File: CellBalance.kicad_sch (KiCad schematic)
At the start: 8 parts, among them Q1 GSF3400

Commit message: mostly done afe ic
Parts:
- removed C1: 10nF, symbol Device:C_Small
- removed D1: BZT52B3V9-AQ, footprints:P35_SOD-123F, symbol symbols:Diode
- removed Q1: GSF3400, Package_TO_SOT_SMD:SOT-23-3, symbol symbols:GSF3400
- removed R1, R2: 52.3, symbol Device:R_Small_US
- removed R3, R4: 1k, symbol Device:R_Small_US
- removed R5: 2k, symbol Device:R_Small_US
- added C4: 1nF, symbol Device:C_Small
- added C5: 330nF, symbol Device:C_Small
- added D3: BZT52B3V9-AQ, footprints:P35_SOD-123F, symbol symbols:Diode
- added GSF2: MOSFET, P-CH, SINGLE, -4.1A, -30, Package_TO_SOT_SMD:SOT-23-3, symbol symbols:GSF0304
- added R11, R12: 52.3k, symbol Device:R_Small_US
- added R13: 10, symbol Device:R_Small_US
- added R14: 8.3, symbol Device:R_Small_US
- added R15: 2k, symbol Device:R_Small_US
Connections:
- net Battery_Bottom: now also C4.1, R11.2, R12.2, R13.1
- net Battery_Top: now also GSF2.2 (S), R14.2
- net Monitor_Bottom: now also C5.2, R13.2, R15.1
- net Monitor_Top: now also C5.1, D3.2 (C), GSF2.1 (G), R14.1, R15.2
- new net: D3.1 (A), GSF2.3 (D), R11.1, R12.1
- new net GNDREF: C4.2
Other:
- note added: "C2 is C_F, 330nF taken from typical application"
- note added: "C3 = C_EMC (i used typical application)"
- note added: "R6/R7 is R_balance"
- note added: "the typical application didn't include the zener or the current limiting resistor i just included it to clamp vgs"

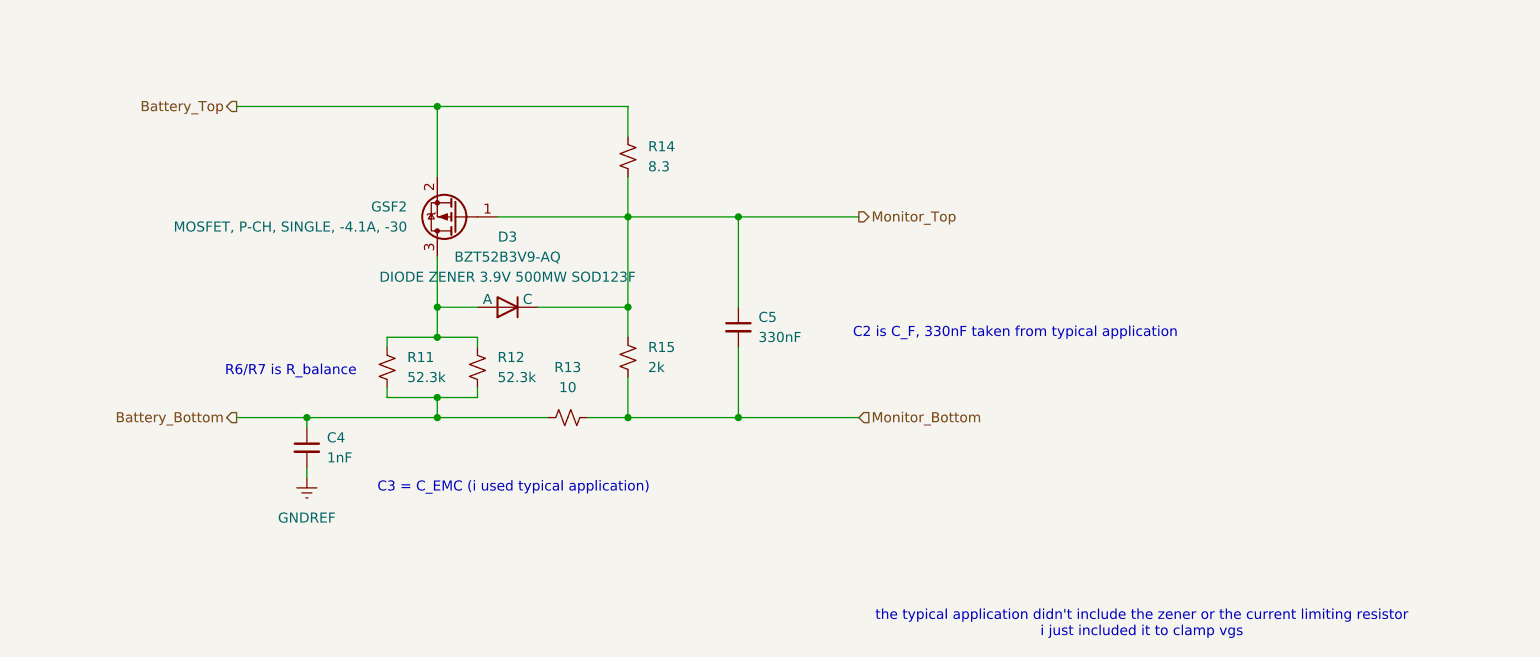
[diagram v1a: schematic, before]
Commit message: fixed balancing module and added pulse transformer
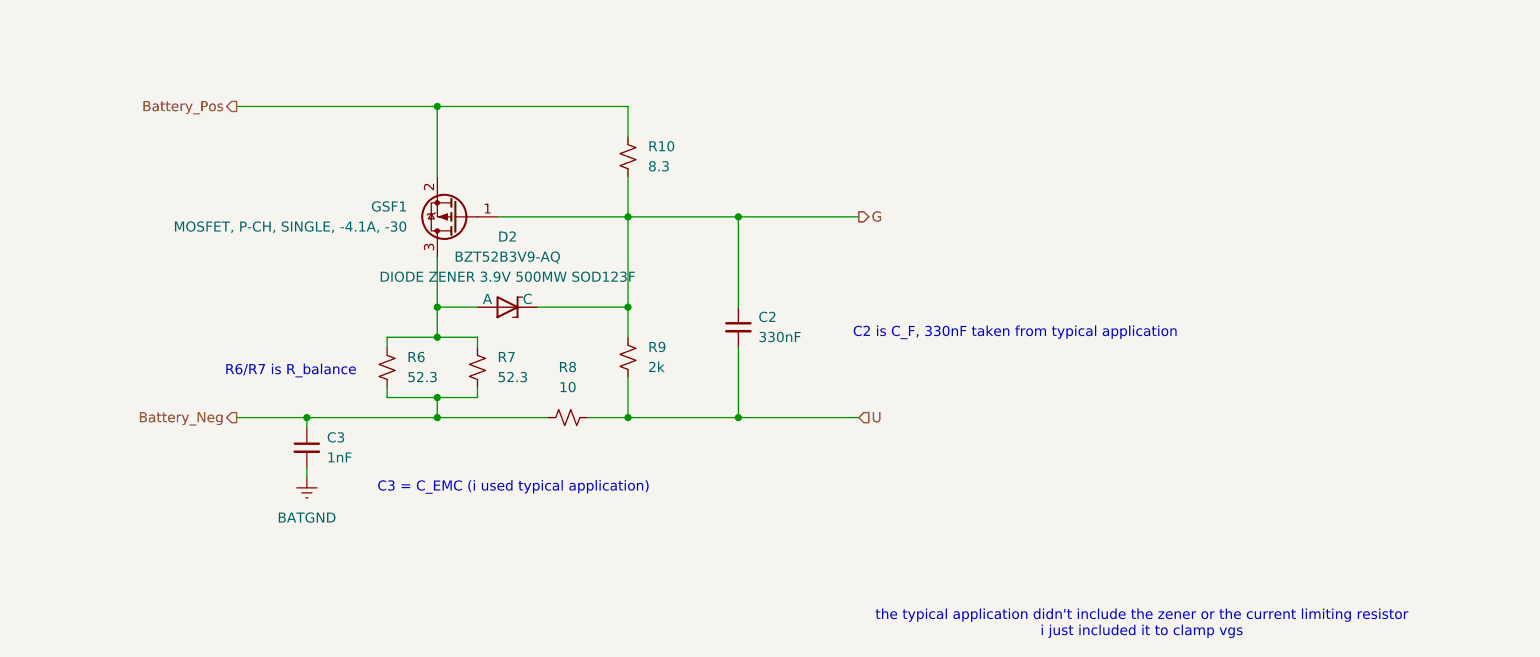
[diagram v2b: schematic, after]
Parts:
- R6: renamed from R11; value 52.3k -> 52.3
- R7: renamed from R12; value 52.3k -> 52.3
- renumbered C5 to C2, C4 to C3, D3 to D2, GSF2 to GSF1, R14 to R10, R13 to R8, R15 to R9
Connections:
- net Battery_Bottom renamed Battery_Neg
- net Battery_Top renamed Battery_Pos
- net GNDREF renamed BATGND
- net Monitor_Bottom renamed U
- net Monitor_Top renamed G

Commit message: finished schematic
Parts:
- removed D2: BZT52B3V9-AQ, footprints:P35_SOD-123F, symbol symbols:Diode
- removed R10: 8.3, symbol Device:R_Small_US
- removed R9: 2k, symbol Device:R_Small_US
- added R8: 8.3, symbol Device:R_Small_US
- C11: renamed from C2; value 330nF -> 100nF
- renumbered C3 to C10, R8 to R9
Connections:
- net Battery_Pos: now also R8.2
- net G: now also R8.1
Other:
- note added: "C2 is C_F, 100nF taken from typical application"
- note removed: "C2 is C_F, 330nF taken from typical application"
- moved on the sheet: C11, GSF1

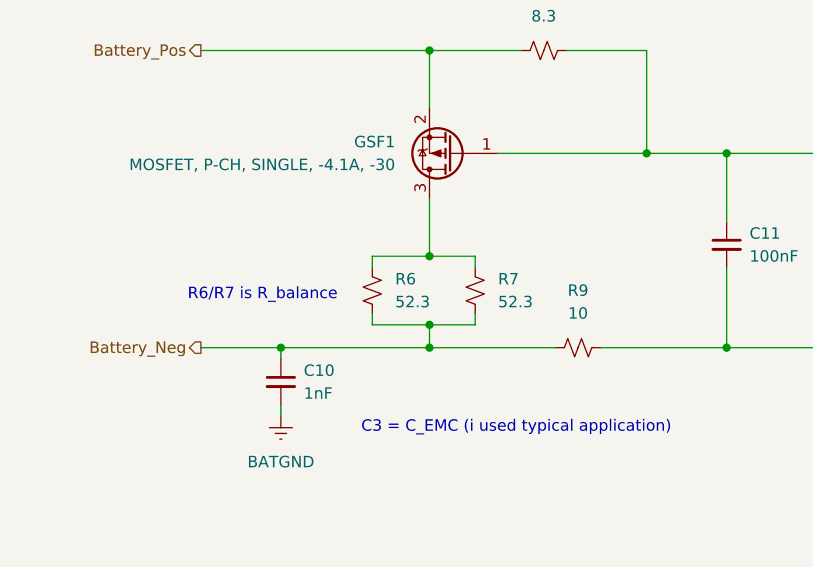
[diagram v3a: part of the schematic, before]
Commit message: added leds and updated library
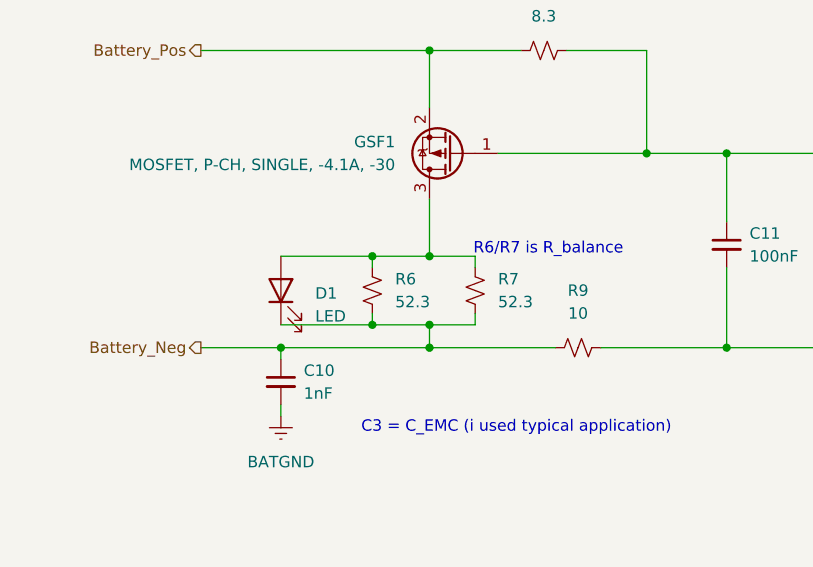
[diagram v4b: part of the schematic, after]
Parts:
- added D1: LED, symbol Device:LED
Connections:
- net Battery_Neg: now also D1.1 (K)
- net at GSF1.3 (D), R6.1, R7.1: now also D1.2 (A)
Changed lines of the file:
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@@
 	(text "R6/R7 is R_balance"
 		(exclude_from_sim no)
-		(at 117.348 99.568 0)
+		(at 149.098 94.488 0)
 		(effects
 			(font
@@
 	)
 	(junction
+		(at 129.54 95.25)
+		(diameter 0)
+		(color 0 0 0 0)
+	)
+	(junction
 		(at 119.38 105.41)
 		(diameter 0)
@@
 	)
 	(junction
+		(at 129.54 102.87)
+		(diameter 0)
+		(color 0 0 0 0)
+	)
+	(junction
 		(at 160.02 83.82)
 		(diameter 0)
@@
 	(wire
 		(pts
+			(xy 119.38 102.87) (xy 129.54 102.87)
+		)
+		(stroke
+			(width 0)
+			(type default)
+		)
+	)
+	(wire
+		(pts
 			(xy 110.49 72.39) (xy 135.89 72.39)
 		)
@@
 		(pts
 			(xy 154.94 105.41) (xy 168.91 105.41)
+		)
+		(stroke
+			(width 0)
+			(type default)
+		)
+	)
+	(wire
+		(pts
+			(xy 119.38 95.25) (xy 129.54 95.25)
 		)
 		(stroke
@@
 					(unit 1)
 				)
+			)
+		)
+	)
+	(symbol
+		(lib_id "Device:LED")
+		(at 119.38 99.06 90)
+		(unit 1)
+		(body_style 1)
+		(exclude_from_sim no)
+		(in_bom yes)
+		(on_board yes)
+		(in_pos_files yes)
+		(dnp no)
+		(fields_autoplaced yes)
+		(property "Reference" "D1"
+			(at 123.19 99.3774 90)
+			(show_name no)
+			(do_not_autoplace no)
+			(effects
+				(font
+					(size 1.27 1.27)
+				)
+				(justify right)
+			)
+		)
+		(property "Value" "LED"
+			(at 123.19 101.9174 90)
+			(show_name no)
+			(do_not_autoplace no)
+			(effects
+				(font
+					(size 1.27 1.27)
+				)
+				(justify right)
+			)
+		)
+		(property "Footprint" ""
+			(at 119.38 99.06 0)
+			(hide yes)
+			(show_name no)
+			(do_not_autoplace no)
+			(effects
+				(font
+					(size 1.27 1.27)
+				)
+			)
+		)
+		(property "Datasheet" "https://www.digikey.ca/en/products/detail/para-light/LC295JRWDT-5A-U1/26692441"
+			(at 119.38 99.06 0)
+			(hide yes)
+			(show_name no)
+			(do_not_autoplace no)
+			(effects
+				(font
+					(size 1.27 1.27)
+				)
+			)
+		)
+		(property "Description" "Light emitting diode"
+			(at 119.38 99.06 0)
+			(hide yes)
+			(show_name no)
+			(do_not_autoplace no)
+			(effects
+				(font
+					(size 1.27 1.27)
+				)
+			)
+		)
+		(property "Sim.Pins" "1=K 2=A"
+			(at 119.38 99.06 0)
+			(hide yes)
+			(show_name no)
+			(do_not_autoplace no)
+			(effects
+				(font
+					(size 1.27 1.27)
+				)
+			)
+		)
+		(pin "1"
+		)
+		(pin "2"
+		)
+		(instances
+			(project "bms-afe"
+				(path "/226a23e7-09bb-40bc-b53a-ec42a6b7cc90/199aea63-5bfb-41be-ba55-0a021bc0a074"
+					(reference "D3")
+					(unit 1)
+				)
+				(path "/226a23e7-09bb-40bc-b53a-ec42a6b7cc90/2aa084bd-01e7-47e5-8f6d-30b4f325d7f4"
+					(reference "D2")
+					(unit 1)
+				)
+				(path "/226a23e7-09bb-40bc-b53a-ec42a6b7cc90/30f9ba51-47e3-4adb-895f-80ddd8089ec1"
+					(reference "D5")
+					(unit 1)
+				)
+				(path "/226a23e7-09bb-40bc-b53a-ec42a6b7cc90/9ef805d4-1601-4480-b9fd-3e26be539576"
+					(reference "D6")
+					(unit 1)
+				)
+				(path "/226a23e7-09bb-40bc-b53a-ec42a6b7cc90/a6f93463-0553-4e94-825f-86704d73fcd7"
+					(reference "D1")
+					(unit 1)
+				)
+				(path "/226a23e7-09bb-40bc-b53a-ec42a6b7cc90/cf97efbe-7ee9-4abe-8844-0d879c082204"
+					(reference "D4")
+					(unit 1)
+				)

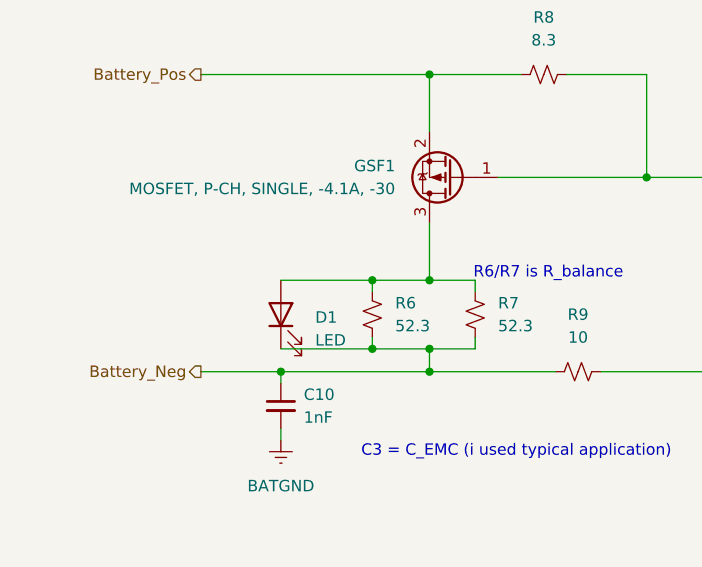
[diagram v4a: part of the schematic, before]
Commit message: added led resistor
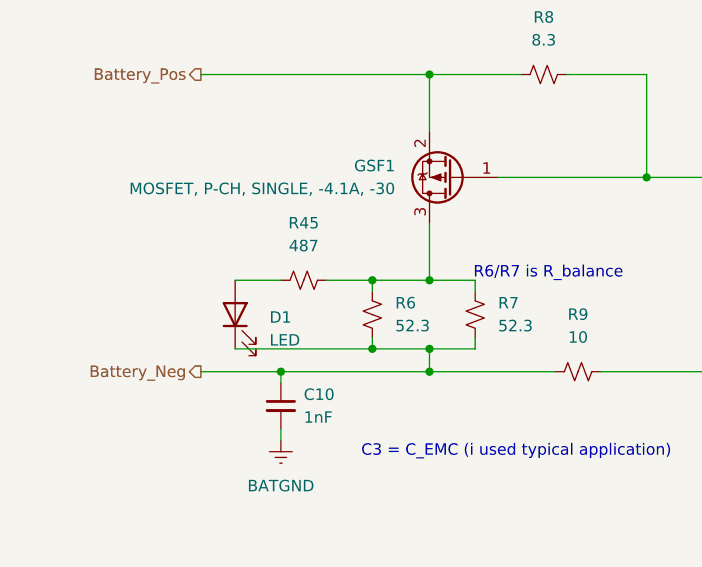
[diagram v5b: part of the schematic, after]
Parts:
- added R45: 487, symbol Device:R_Small_US
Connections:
- net at GSF1.3 (D), R6.1, R7.1: now also R45.2; no longer D1.2 (A)
- new net: D1.2 (A), R45.1
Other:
- moved on the sheet: D1
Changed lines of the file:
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@@
+	)
+	(junction
+		(at 119.38 105.41)
+		(diameter 0)
+		(color 0 0 0 0)
+	)
+	(junction
+		(at 135.89 105.41)
+		(diameter 0)
+		(color 0 0 0 0)
+	)
+	(junction
+		(at 129.54 102.87)
+		(diameter 0)
+		(color 0 0 0 0)
+	)
+	(junction
+		(at 160.02 83.82)
+		(diameter 0)
+		(color 0 0 0 0)
 	)
 	(junction
@@
 		(color 0 0 0 0)
 	)
-	(junction
-		(at 119.38 105.41)
-		(diameter 0)
-		(color 0 0 0 0)
-	)
-	(junction
-		(at 135.89 105.41)
-		(diameter 0)
-		(color 0 0 0 0)
-	)
-	(junction
-		(at 129.54 102.87)
-		(diameter 0)
-		(color 0 0 0 0)
-	)
-	(junction
-		(at 160.02 83.82)
-		(diameter 0)
-		(color 0 0 0 0)
-	)
 	(wire
 		(pts
@@
 	(wire
 		(pts
-			(xy 119.38 102.87) (xy 129.54 102.87)
+			(xy 114.3 102.87) (xy 129.54 102.87)
 		)
 		(stroke
@@
 	(wire
 		(pts
-			(xy 119.38 95.25) (xy 129.54 95.25)
+			(xy 114.3 95.25) (xy 119.38 95.25)
 		)
 		(stroke
@@
 		(pts
 			(xy 168.91 83.82) (xy 168.91 91.44)
+		)
+		(stroke
+			(width 0)
+			(type default)
+		)
+	)
+	(wire
+		(pts
+			(xy 124.46 95.25) (xy 129.54 95.25)
 		)
 		(stroke
@@
 	)
 	(symbol
+		(lib_id "Device:R_Small_US")
+		(at 121.92 95.25 90)
+		(unit 1)
+		(body_style 1)
+		(exclude_from_sim no)
+		(in_bom yes)
+		(on_board yes)
+		(in_pos_files yes)
+		(dnp no)
+		(fields_autoplaced yes)
+		(property "Reference" "R45"
+			(at 121.92 88.9 90)
+			(show_name no)
+			(do_not_autoplace no)
+			(effects
+				(font
+					(size 1.27 1.27)
+				)
+			)
+		)
+		(property "Value" "487"
+			(at 121.92 91.44 90)
+			(show_name no)
+			(do_not_autoplace no)
+			(effects
+				(font
+					(size 1.27 1.27)
+				)
+			)
+		)
+		(property "Footprint" ""
+			(at 121.92 95.25 0)
+			(hide yes)
+			(show_name no)
+			(do_not_autoplace no)
+			(effects
+				(font
+					(size 1.27 1.27)
+				)
+			)
+		)
+		(property "Datasheet" ""
+			(at 121.92 95.25 0)
+			(hide yes)
+			(show_name no)
+			(do_not_autoplace no)
+			(effects
+				(font
+					(size 1.27 1.27)
+				)
+			)
+		)
+		(property "Description" "Resistor, small US symbol"
+			(at 121.92 95.25 0)
+			(hide yes)
+			(show_name no)
+			(do_not_autoplace no)
+			(effects
+				(font
+					(size 1.27 1.27)
+				)
+			)
+		)
+		(pin "2"
+		)
+		(pin "1"
+		)
+		(instances
+			(project "bms-afe"
+				(path "/226a23e7-09bb-40bc-b53a-ec42a6b7cc90/199aea63-5bfb-41be-ba55-0a021bc0a074"
+					(reference "R47")
+					(unit 1)
+				)
+				(path "/226a23e7-09bb-40bc-b53a-ec42a6b7cc90/2aa084bd-01e7-47e5-8f6d-30b4f325d7f4"
+					(reference "R46")
+					(unit 1)
+				)
+				(path "/226a23e7-09bb-40bc-b53a-ec42a6b7cc90/30f9ba51-47e3-4adb-895f-80ddd8089ec1"
+					(reference "R49")
+					(unit 1)
+				)
+				(path "/226a23e7-09bb-40bc-b53a-ec42a6b7cc90/9ef805d4-1601-4480-b9fd-3e26be539576"
+					(reference "R50")
+					(unit 1)
+				)
+				(path "/226a23e7-09bb-40bc-b53a-ec42a6b7cc90/a6f93463-0553-4e94-825f-86704d73fcd7"
+					(reference "R45")
+					(unit 1)
+				)
+				(path "/226a23e7-09bb-40bc-b53a-ec42a6b7cc90/cf97efbe-7ee9-4abe-8844-0d879c082204"
+					(reference "R48")
+					(unit 1)
+				)
+			)
+		)
+	)
+	(symbol
 		(lib_id "Device:LED")
-		(at 119.38 99.06 90)
+		(at 114.3 99.06 90)
 		(unit 1)
 		(body_style 1)
@@
 		(fields_autoplaced yes)
 		(property "Reference" "D1"
-			(at 123.19 99.3774 90)
+			(at 118.11 99.3774 90)
 			(show_name no)
 			(do_not_autoplace no)
@@
 		)
 		(property "Value" "LED"
-			(at 123.19 101.9174 90)
+			(at 118.11 101.9174 90)
 			(show_name no)
 			(do_not_autoplace no)
@@
 		)
 		(property "Footprint" ""
-			(at 119.38 99.06 0)
+			(at 114.3 99.06 0)
 			(hide yes)
 			(show_name no)
@@
 		)
 		(property "Datasheet" "https://www.digikey.ca/en/products/detail/para-light/LC295JRWDT-5A-U1/26692441"
-			(at 119.38 99.06 0)
+			(at 114.3 99.06 0)
 			(hide yes)
 			(show_name no)
@@
 		)
 		(property "Description" "Light emitting diode"
-			(at 119.38 99.06 0)
+			(at 114.3 99.06 0)
 			(hide yes)
 			(show_name no)
@@
 		)
 		(property "Sim.Pins" "1=K 2=A"
-			(at 119.38 99.06 0)
-			(hide yes)
-			(show_name no)
+			(at 114.3 99.06 0)
+			(hide yes)
+			(show_name no)

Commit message: fixed minor changes
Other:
- note added: "= C_EMC (i used typical application)"
- note added: "Bleed resistors"
- note added: "C_F is placed on top level"
- note removed: "C2 is C_F, 100nF taken from typical application"
- note removed: "C3 = C_EMC (i used typical application)"
- note removed: "R6/R7 is R_balance"
- note removed: "the typical application didn't include the zener or the current limiting resistor i just included it to clamp vgs"
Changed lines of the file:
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@@
 	(generator_version "10.0")
 	(paper "A4")
-	(text "C3 = C_EMC (i used typical application)"
+	(text "= C_EMC (i used typical application)"
 		(exclude_from_sim no)
-		(at 145.542 114.3 0)
+		(at 144.78 109.22 0)
 		(effects
 			(font
@@
 		)
 	)
-	(text "C2 is C_F, 100nF taken from typical application"
+	(text "C_F is placed on top level"
 		(exclude_from_sim no)
 		(at 209.042 94.742 0)
@@
 		)
 	)
-	(text "the typical application didn't include the zener or the current limiting resistor\ni just included it to clamp vgs"
+	(text "Bleed resistors"
 		(exclude_from_sim no)
-		(at 225.044 131.572 0)
+		(at 149.606 95.504 0)
 		(effects
 			(font
-				(size 1.27 1.27)
-			)
-		)
-	)
-	(text "R6/R7 is R_balance"
-		(exclude_from_sim no)
-		(at 149.098 94.488 0)
-		(effects
-			(font

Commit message: passive values
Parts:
- removed C11: 100nF, symbol Device:C_Small
- added C35: CAP CER 0.1UF 25V X7R 0603, Capacitor_SMD:C_0603_1608Metric, symbol Device:C_Small
- C10: value 1nF -> CAP CER 0603 1NF 16V X7R 10%; footprint (none) -> Capacitor_SMD:C_0603_1608Metric
- D1: value LED -> 1.6X0.8MM RED/WHT SMD LED; footprint (none) -> Diode_SMD:D_0603_1608Metric
- R45: value 487 -> RES SMD 487 OHM 1% 1/10W 0603; footprint (none) -> Capacitor_SMD:C_0603_1608Metric
- R6, R7: value 52.3 -> RES SMD 52.3 OHM 1% 1/2W 1210; footprint (none) -> Capacitor_SMD:C_1210_3225Metric
- R8: value 8.3 -> RES SMD 8.2 OHM 1% 1/8W 0603; footprint (none) -> Capacitor_SMD:C_0603_1608Metric
- R9: value 10 -> RES 10 OHM 1% 1/10W 0603; footprint (none) -> Resistor_SMD:R_0603_1608Metric
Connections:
- net BATGND: now also C10.1; no longer C10.2
- net Battery_Neg: now also C10.2; no longer C10.1
- net G: now also C35.1
- net U: now also C35.2
